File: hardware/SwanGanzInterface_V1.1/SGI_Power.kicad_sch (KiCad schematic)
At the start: 25 parts, among them J1 2479774-1, Q1 SQ2389CES-T1_GE3, SW1 Power_Switch, U1 LM2937ET-3.3_NOPB, U2 LM4041CILPR, U3 OPA2350

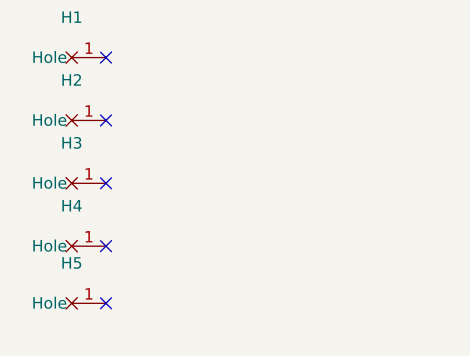
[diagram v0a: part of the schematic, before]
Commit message: Pin Allocation, updated schematic with new pins, reassigned
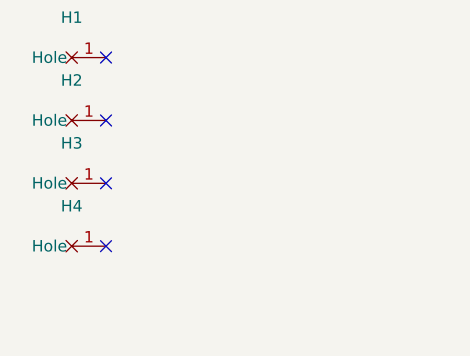
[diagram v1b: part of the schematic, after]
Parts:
- removed H5: ~, SGI_FootprintsLib:MountingHole_4_40, symbol SGI_SymbolLib:MountingHole
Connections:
- no-connect marks 9 -> 8
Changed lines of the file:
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@@
 	)
 	(no_connect
-		(at 27.305 129.54)
-	)
-	(no_connect
 		(at 27.305 109.22)
 	)
@@
 					(unit 1)
 				)
-			)
-		)
-	)
-	(symbol
-		(lib_id "SGI_SymbolLib:MountingHole")
-		(at 27.305 129.54 0)
-		(unit 1)
-		(exclude_from_sim no)
-		(in_bom yes)
-		(on_board yes)
-		(dnp no)
-		(fields_autoplaced yes)
-		(property "Reference" "H5"
-			(at 23.495 125.095 0)
-			(effects
-				(font
-					(size 1.27 1.27)
-				)
-			)
-		)
-		(property "Value" "~"
-			(at 23.495 127.635 0)
-			(effects
-				(font
-					(size 1.27 1.27)
-				)
-			)
-		)
-		(property "Footprint" "SGI_FootprintsLib:MountingHole_4_40"
-			(at 27.305 129.54 0)
-			(effects
-				(font
-					(size 1.27 1.27)
-				)
-				(hide yes)
-			)
-		)
-		(property "Datasheet" ""
-			(at 27.305 129.54 0)
-			(effects
-				(font
-					(size 1.27 1.27)
-				)
-				(hide yes)
-			)
-		)
-		(property "Description" "Drill hole for 4-40 screw"
-			(at 27.305 129.54 0)
-			(effects
-				(font
-					(size 1.27 1.27)
-				)
-				(hide yes)
-			)
-		)
-		(pin "1"
-		)
-		(instances
-			(project "SwanGanzInterface"
-				(path "/4e9a6e30-f660-472b-9696-bea1f34b4545/090a1e64-9482-4912-b352-6eea35714559"
-					(reference "H5")
-					(unit 1)
-				)

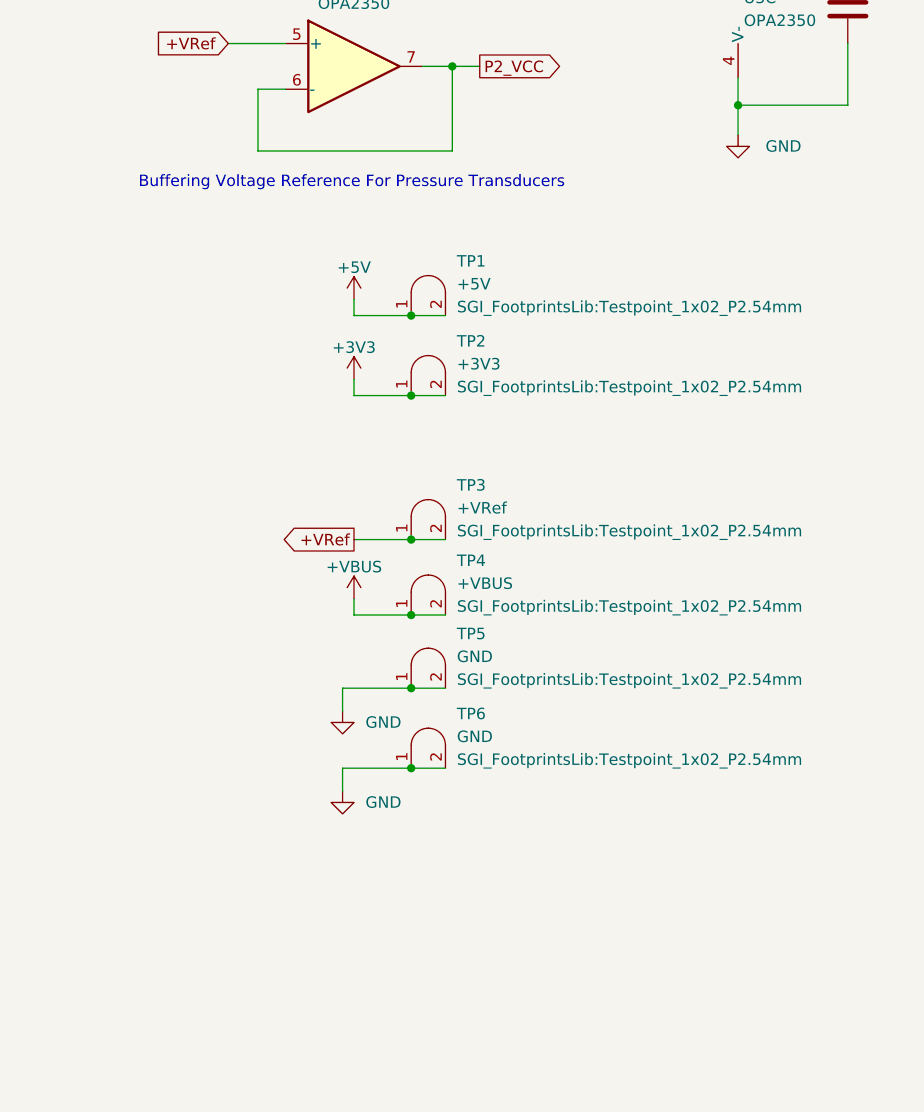
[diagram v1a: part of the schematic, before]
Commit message: Started converting things to use touch screen chip
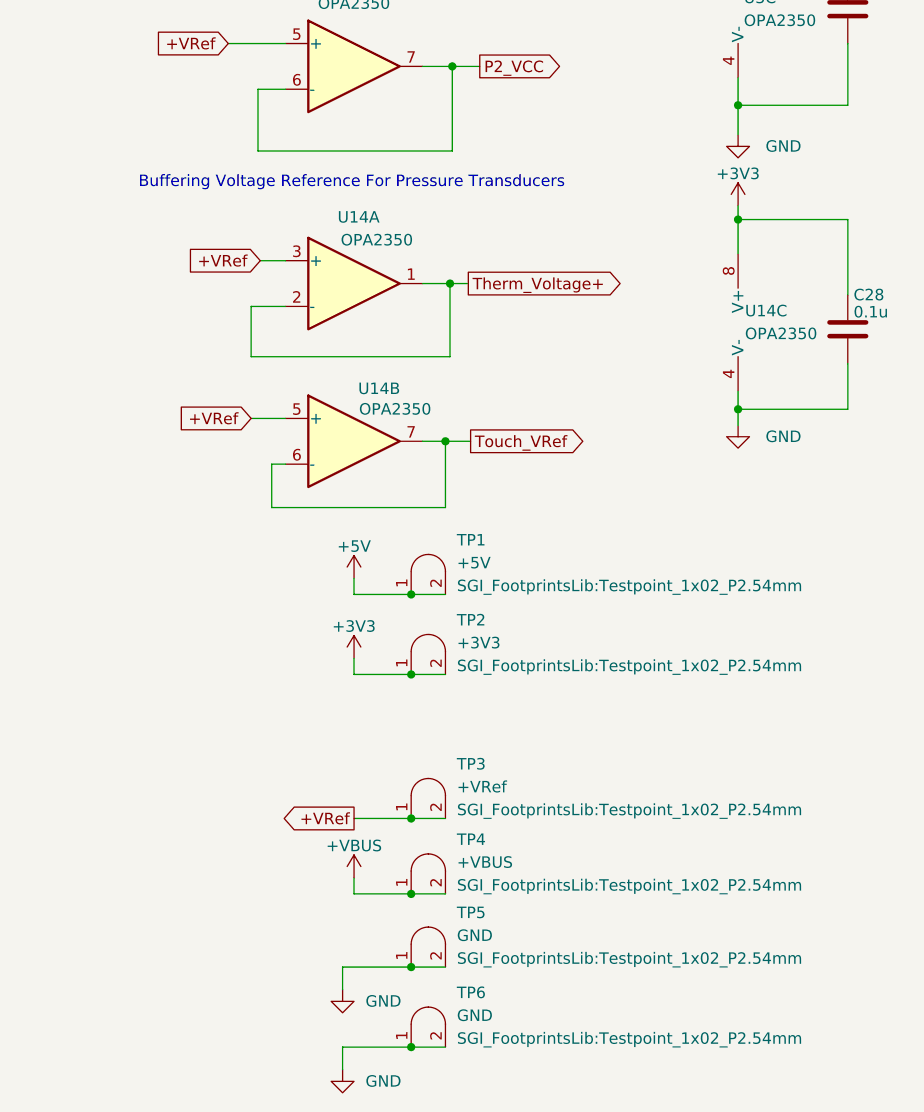
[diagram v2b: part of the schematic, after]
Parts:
- added C28: 0.1u, Capacitor_SMD:C_0603_1608Metric, symbol Device:C
- added U14: OPA2350, Package_DIP:DIP-8_W7.62mm, symbol SGI_SymbolLib:OPA2350PA
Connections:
- net +3V3: now also C28.1, U14.8 (V+)
- net +VRef: now also U14.3 (+), U14.5 (+)
- net GND: now also C28.2, U14.4 (V-)
- new net Therm_Voltage+: U14.1, U14.2 (-)
- new net Touch_VRef: U14.6 (-), U14.7
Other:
- moved on the sheet: TP1, TP2, TP3, TP4, TP5, TP6

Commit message: Added lots, moving to 64 pin micro
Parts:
- removed J1: 2479774-1, SGI_FootprintsLib:24797741, symbol SGI_SymbolLib:2479774-1
- removed R1, R2: 5k1, Resistor_SMD:R_0603_1608Metric, symbol Device:R
- added J1: Conn_01x02_Pin, symbol Connector:Conn_01x02_Pin
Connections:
- net +VBUS: now also J1.1 (Pin_1)
- net GND: now also J1.2 (Pin_2)
- no-connect marks 8 -> 4
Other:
- note removed: "USB-C Power"
